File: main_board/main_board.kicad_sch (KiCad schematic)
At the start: 78 parts, among them J18 Conn_01x15_Female, J19 Conn_01x15_Female, J20 Conn_01x02_Male, J21 OLED Pins, J5 Display Header, J6 EU Power, J7 Expansion Header, M1 OLED, SW10 Push Button, SW11 Push Button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

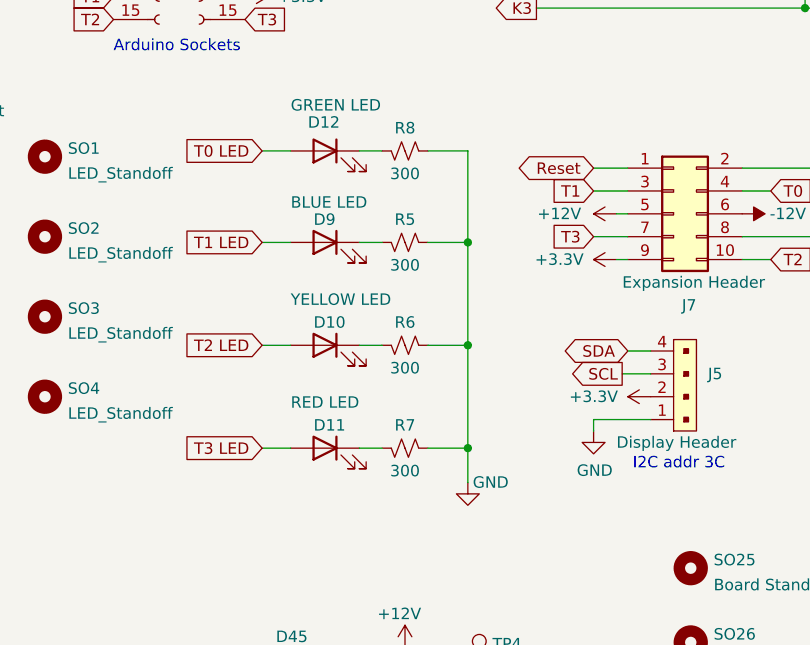
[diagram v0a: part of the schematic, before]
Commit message: Fixes main board.
Fixes regulator footprint. Re lays out board to improve noise performance. Around -50db now at outputs.
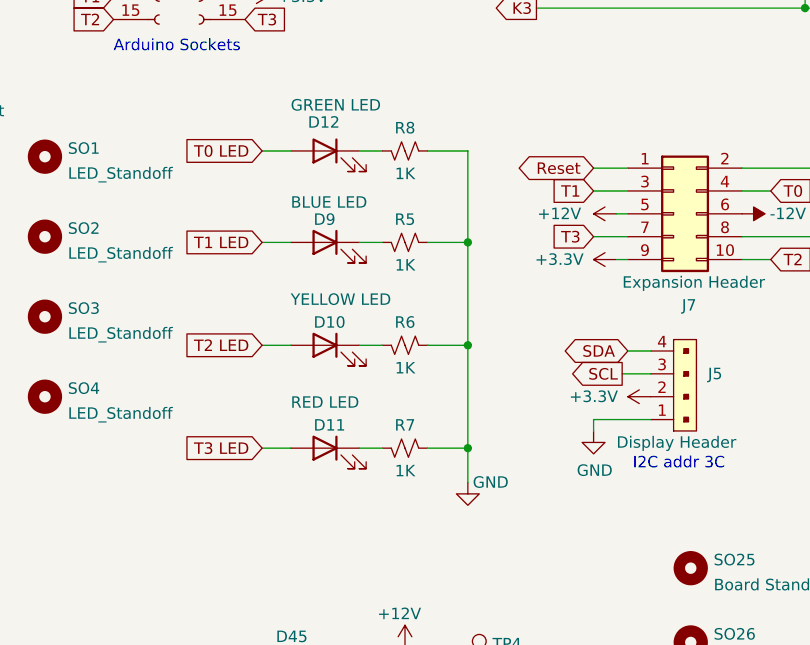
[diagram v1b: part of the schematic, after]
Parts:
- D10: Digi-Key Part 160-1961-ND -> 732-5010-ND
- D12: Digi-Key Part 732-5008-ND -> 732-5007-ND
- R5, R6, R7, R8: value 300 -> 1K; Digi-Key Part 311-10KARCT-ND -> RNCP0805FTD1K00CT-ND; LCSC Part # C17617 -> C17513

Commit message: Updates bom for digi-key
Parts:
- C1, C2: Digi-Key Part 399-EDH107M016A9GAACT-ND -> 399-A768EB107M1ELAE036DKR-ND
- C7: Digi-Key Part 311-1888-1-ND -> 1276-1029-1-ND
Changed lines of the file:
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@@
       (effects (font (size 1.27 1.27)) hide)
     )
-    (property "Digi-Key Part" "311-1888-1-ND" (id 4) (at 57.15 23.495 0)
+    (property "Digi-Key Part" "1276-1029-1-ND" (id 4) (at 57.15 23.495 0)
       (effects (font (size 1.27 1.27)) hide)
     )
@@
       (effects (font (size 1.27 1.27)) hide)
     )
-    (property "Digi-Key Part" "399-EDH107M016A9GAACT-ND" (id 4) (at 122.555 147.955 0)
+    (property "Digi-Key Part" "399-A768EB107M1ELAE036DKR-ND" (id 4) (at 122.555 147.955 0)
       (effects (font (size 1.27 1.27)) hide)
     )
@@
       (effects (font (size 1.27 1.27)) hide)
     )
-    (property "Digi-Key Part" "399-EDH107M016A9GAACT-ND" (id 4) (at 122.555 158.75 0)
-      (effects (font (size 1.27 1.27)) hide)
-    )
+    (property "Digi-Key Part" "399-A768EB107M1ELAE036DKR-ND" (id 4) (at 122.555 158.75 0)
+      (effects (font (size 1.27 1.27)) hide)
+    )
